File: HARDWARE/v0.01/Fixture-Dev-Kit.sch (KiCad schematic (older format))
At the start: 0 parts

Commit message: addin more circuits!
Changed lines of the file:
@@
 $Descr A4 11693 8268
 encoding utf-8
-Sheet 1 7
+Sheet 1 9
 Title ""
 Date ""
@@
 F1 "Fixture-Dev-Kit_DUT.sch" 60
 $EndSheet
+$Sheet
+S 6200 3750 1150 850
+U 59EF8AA8
+F0 "Fixture Dev Kit - IO Expander" 60
+F1 "FixtureDevKit-IOExpander.sch" 60
+$EndSheet
+$Sheet
+S 6300 5050 1150 800
+U 59EFF8A7
+F0 "Fixture Dev Kit - Mosfets" 61
+F1 "FixtureDevKit-Mosfet.sch" 61
+$EndSheet
 $EndSCHEMATC

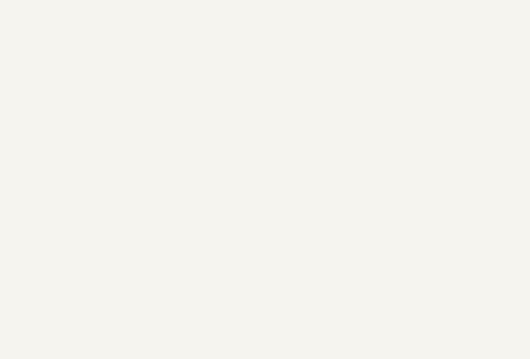
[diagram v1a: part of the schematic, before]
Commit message: adding netlist and design rules check
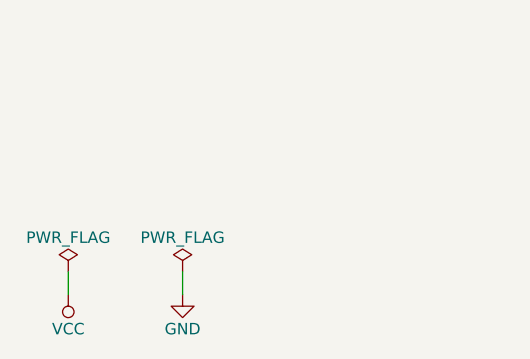
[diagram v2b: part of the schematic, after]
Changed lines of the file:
@@
 F1 "FixtureDevKit-Mosfet.sch" 61
 $EndSheet
+$Comp
+L PWR_FLAG #FLG01
+U 1 1 59EFDEB7
+P 800 7350
+F 0 "#FLG01" H 800 7425 50  0001 C CNN
+F 1 "PWR_FLAG" H 800 7500 50  0000 C CNN
+F 2 "" H 800 7350 50  0001 C CNN
+F 3 "" H 800 7350 50  0001 C CNN
+	1    800  7350
+	1    0    0    -1
+$EndComp
+$Comp
+L PWR_FLAG #FLG02
+U 1 1 59EFDEC9
+P 1300 7350
+F 0 "#FLG02" H 1300 7425 50  0001 C CNN
+F 1 "PWR_FLAG" H 1300 7500 50  0000 C CNN
+F 2 "" H 1300 7350 50  0001 C CNN
+F 3 "" H 1300 7350 50  0001 C CNN
+	1    1300 7350
+	1    0    0    -1
+$EndComp
+$Comp
+L GND #PWR03
+U 1 1 59EFDED6
+P 1300 7450
+F 0 "#PWR03" H 1300 7200 50  0001 C CNN
+F 1 "GND" H 1300 7300 50  0000 C CNN
+F 2 "" H 1300 7450 50  0001 C CNN
+F 3 "" H 1300 7450 50  0001 C CNN
+	1    1300 7450
+	1    0    0    -1
+$EndComp
+$Comp
+L VCC #PWR04
+U 1 1 59EFDEEA
+P 800 7450
+F 0 "#PWR04" H 800 7300 50  0001 C CNN
+F 1 "VCC" H 800 7600 50  0000 C CNN
+F 2 "" H 800 7450 50  0001 C CNN
+F 3 "" H 800 7450 50  0001 C CNN
+	1    800  7450
+	-1   0    0    1
+$EndComp
+Wire Wire Line
+	800  7350 800  7450
+Wire Wire Line
+	1300 7350 1300 7450
 $EndSCHEMATC
